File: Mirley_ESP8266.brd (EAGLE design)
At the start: 52 x 69.4 mm, 71 parts, among them J1 61301611121, J2 61301611121, T10 BC817U, T11 BC817U, T12 BC817U, T13 BC817U, T14 BC817U, T7 BC817U, T8 BC817U, T9 BC817U

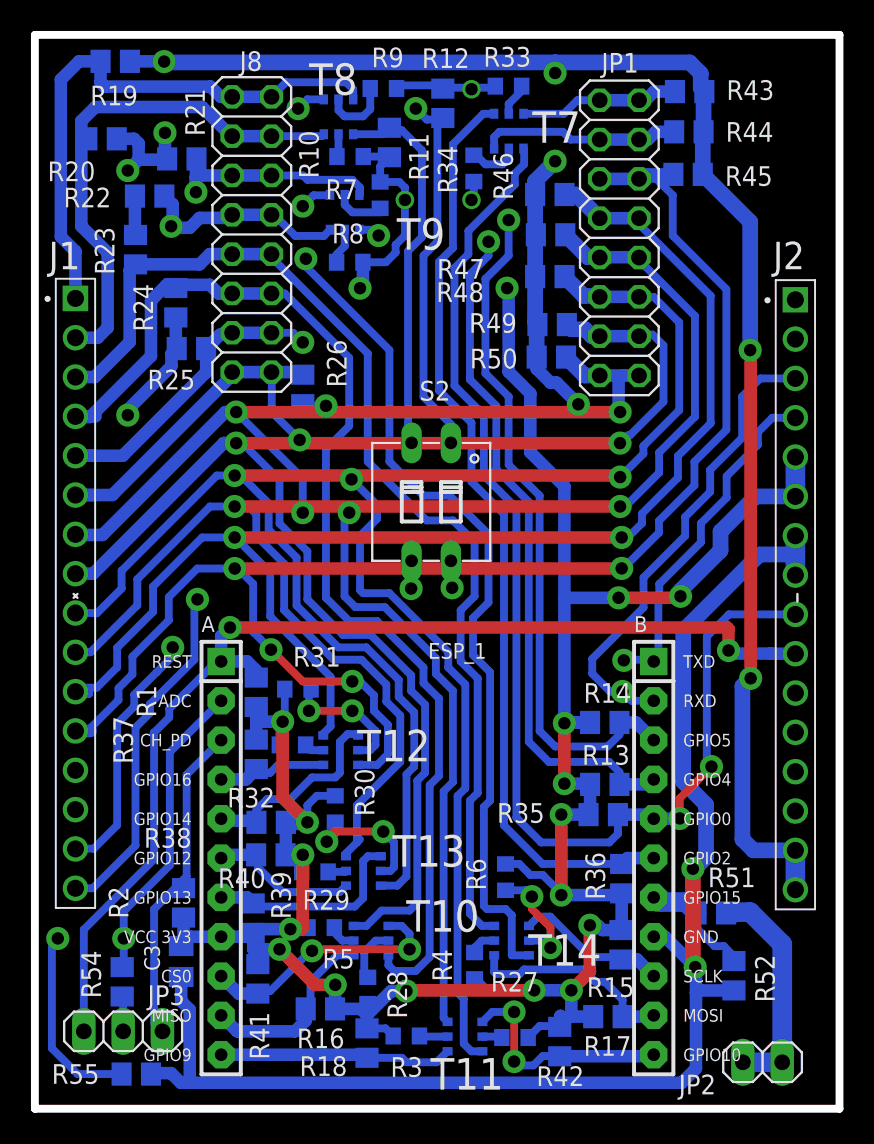
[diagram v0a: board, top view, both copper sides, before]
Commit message: powiekszonyy odstepy miedzy sciezkami
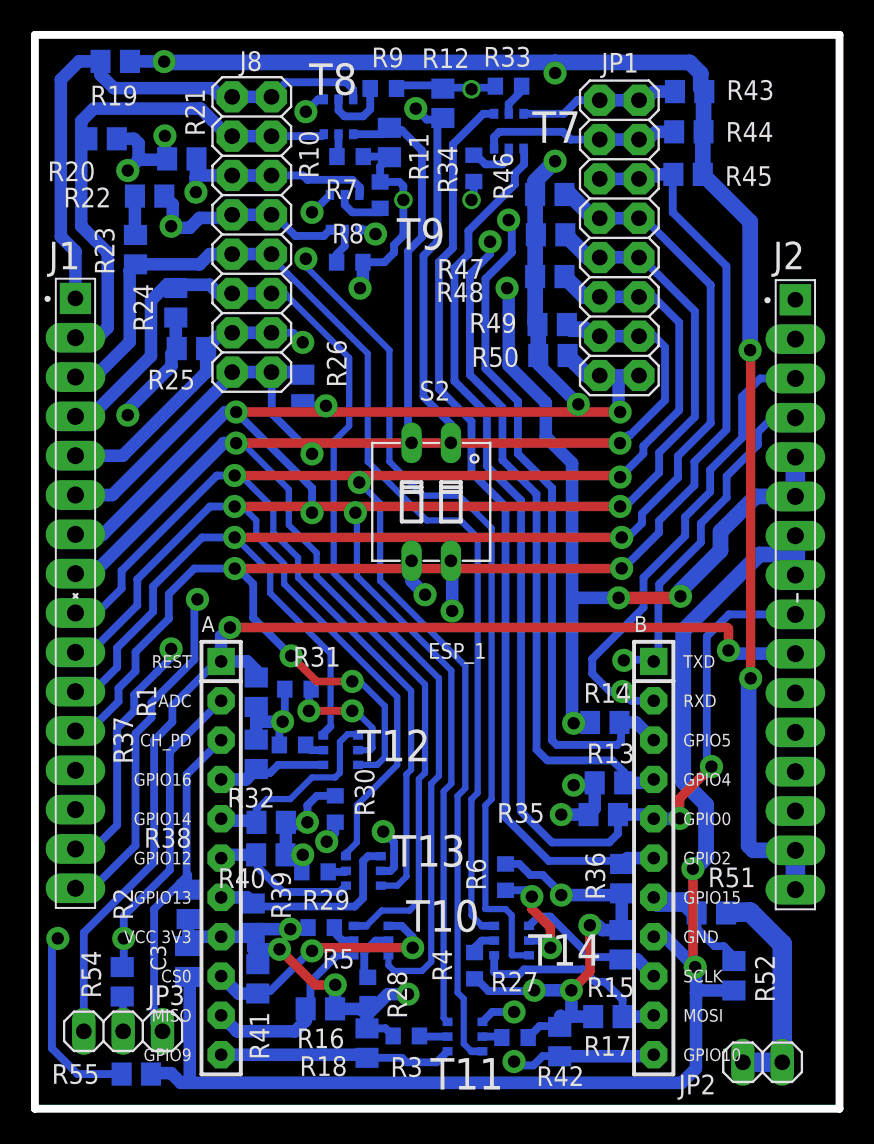
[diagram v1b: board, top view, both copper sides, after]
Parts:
- moved C3 0.40 mm to (9.85, 9.51)
- moved R2 0.32 mm to (9.90, 13.2)
- moved R13 0.32 mm to (37.1, 21.1)
- moved R50 0.14 mm to (33.5, 48.6)
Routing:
- net +3V3: track 189.3 -> 157.2 mm
- net N$22: track 9.15 -> 5.17 mm
- net GPIO10: track 15.1 -> 12.0 mm
- net LED_A2: track 95.9 -> 94.2 mm
- net TXD: track 32.5 -> 34.0 mm
- net LL7: track 92.9 -> 91.5 mm
- net LL4: track 75.0 -> 73.7 mm
- net LED_A1: track 94.5 -> 93.2 mm
- net LL6: track 67.7 -> 66.6 mm
- net LL8: track 94.1 -> 93.1 mm
- net +5V: track 132.5 -> 131.7 mm
- net RXD: track 25.0 -> 25.8 mm
- net LED_A4: track 99.4 -> 98.8 mm
- net ENABLE: track 21.4 -> 21.9 mm
- net LL3: track 70.7 -> 70.2 mm

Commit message: zmniejszona szerokosc sciezek pod tranzystorami
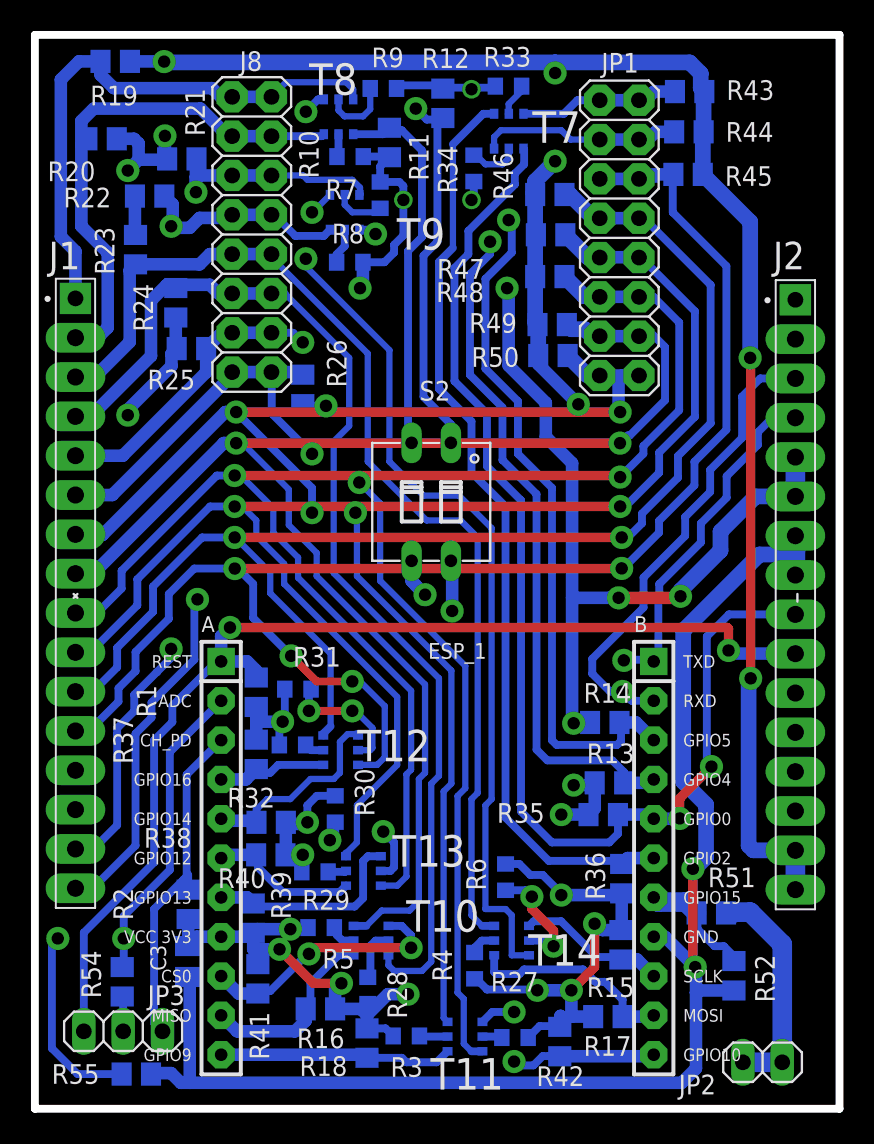
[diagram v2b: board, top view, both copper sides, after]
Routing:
- net +3V3: track 157.2 -> 158.0 mm
